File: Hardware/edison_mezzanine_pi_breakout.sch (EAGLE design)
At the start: 46 parts, among them U1 PCA9306, U2 EDISON_CONNECTOR_FULLMOUNTING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, U3 EDISON_CONNECTOR_FULLHEADER, U4 TPS62065, U5 MIC5219 3.3V

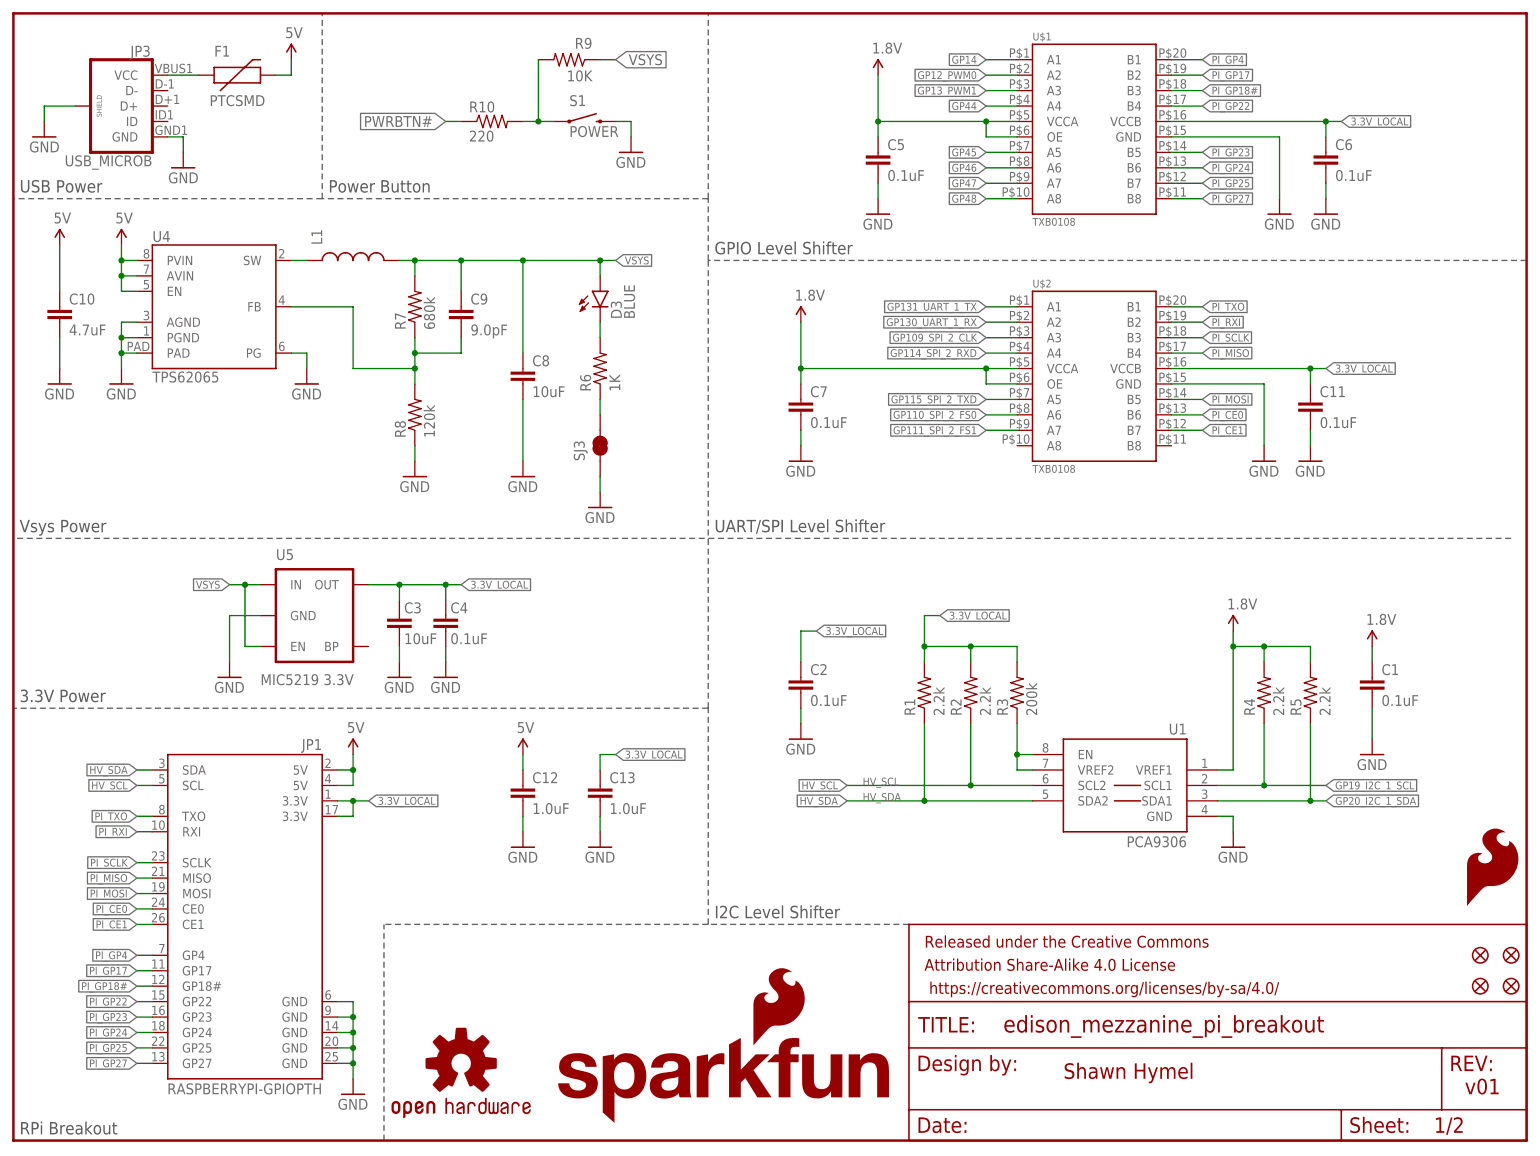
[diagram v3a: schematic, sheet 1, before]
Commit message: Added LED EN to silk. Enlargened section headings on schem.
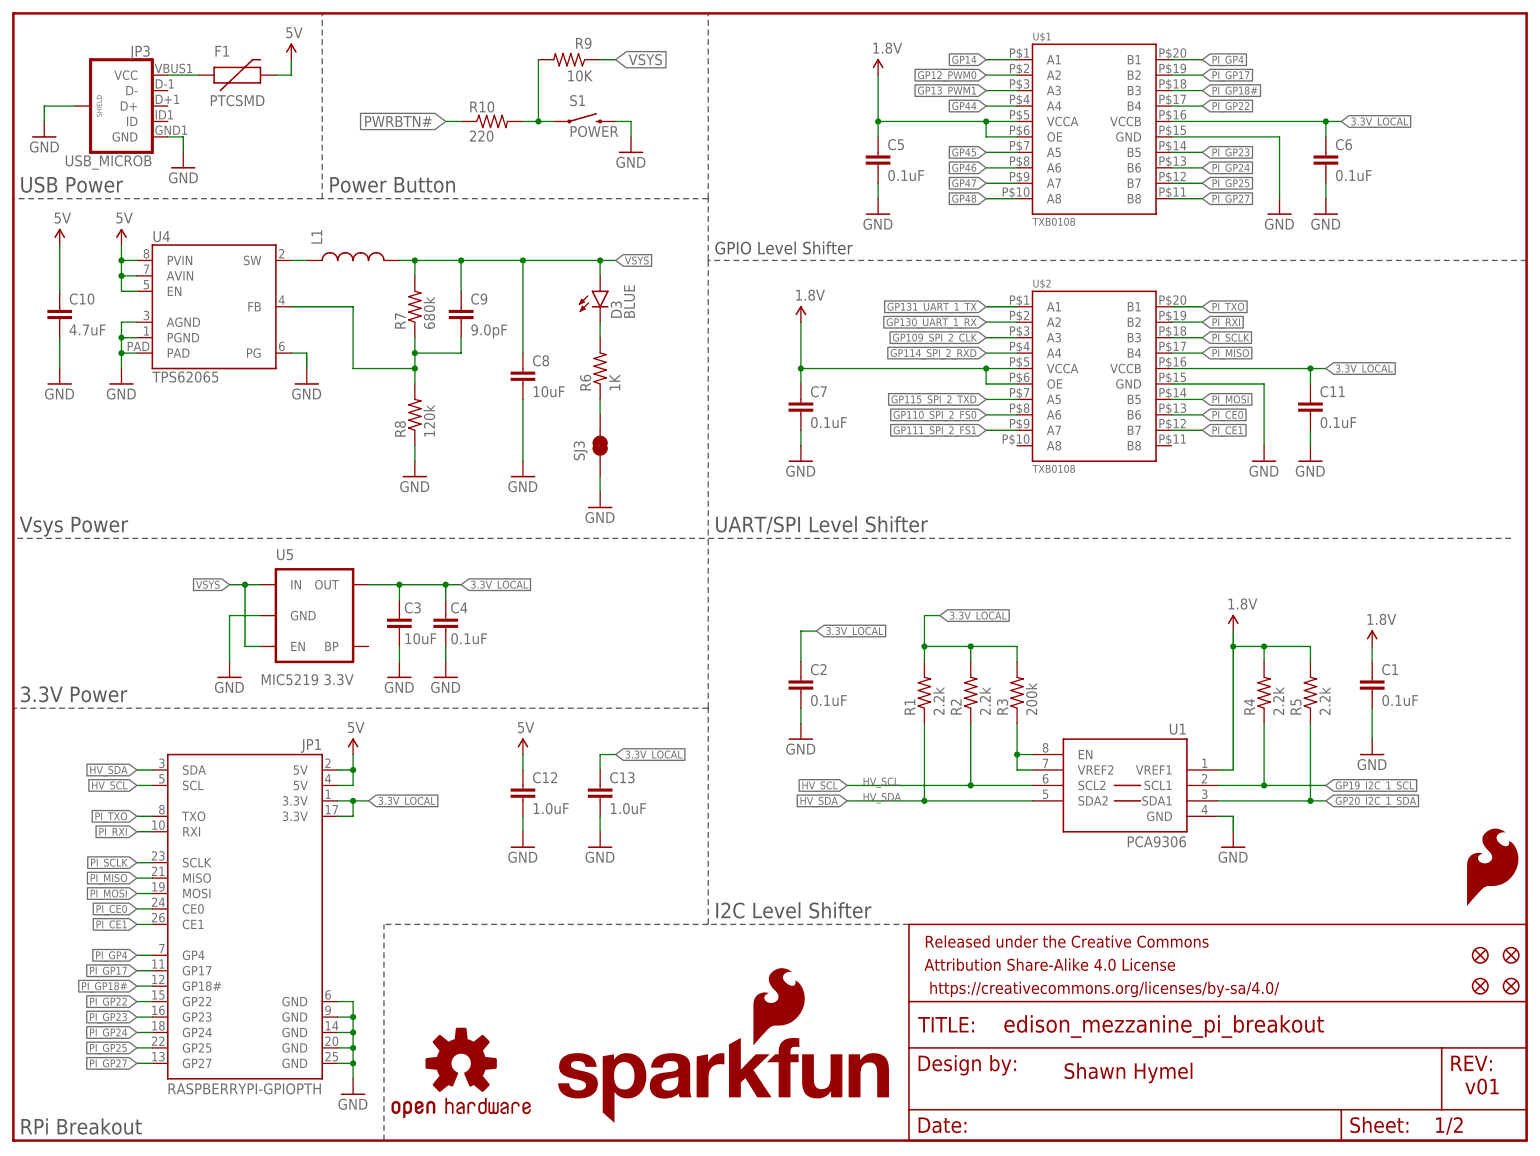
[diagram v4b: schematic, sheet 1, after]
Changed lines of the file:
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@@
 <wire x1="246.38" y1="99.06" x2="0" y2="99.06" width="0.1524" layer="97" style="longdash"/>
 <wire x1="248.92" y1="144.78" x2="114.3" y2="144.78" width="0.1524" layer="97" style="longdash"/>
-<text x="1.016" y="155.956" size="2.032" layer="97">USB Power</text>
-<text x="1.016" y="100.076" size="2.032" layer="97">Vsys Power</text>
-<text x="1.016" y="72.136" size="2.032" layer="97">3.3V Power</text>
-<text x="1.016" y="1.016" size="2.032" layer="97">RPi Breakout</text>
+<text x="1.016" y="155.956" size="2.54" layer="97">USB Power</text>
+<text x="1.016" y="100.076" size="2.54" layer="97">Vsys Power</text>
+<text x="1.016" y="72.136" size="2.54" layer="97">3.3V Power</text>
+<text x="1.016" y="1.016" size="2.54" layer="97">RPi Breakout</text>
 <text x="115.316" y="145.796" size="2.032" layer="97">GPIO Level Shifter</text>
-<text x="115.316" y="100.076" size="2.032" layer="97">UART/SPI Level Shifter</text>
-<text x="115.316" y="36.576" size="2.032" layer="97">I2C Level Shifter</text>
+<text x="115.316" y="100.076" size="2.54" layer="97">UART/SPI Level Shifter</text>
+<text x="115.316" y="36.576" size="2.54" layer="97">I2C Level Shifter</text>
 <wire x1="147.32" y1="35.56" x2="114.3" y2="35.56" width="0.1524" layer="97" style="longdash"/>
 <wire x1="114.3" y1="35.56" x2="60.96" y2="35.56" width="0.1524" layer="97" style="longdash"/>
 <wire x1="60.96" y1="0" x2="60.96" y2="35.56" width="0.1524" layer="97" style="longdash"/>
 <wire x1="50.8" y1="154.94" x2="50.8" y2="185.42" width="0.1524" layer="97" style="longdash"/>
-<text x="51.816" y="155.956" size="2.032" layer="97">Power Button</text>
+<text x="51.816" y="155.956" size="2.54" layer="97">Power Button</text>
 </plain>
 <instances>
